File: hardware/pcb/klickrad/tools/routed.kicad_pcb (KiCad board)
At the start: 2 copper layers, 32 x 32 mm, 25 parts, among them J1 SM06B-SRSS-TB, SW1 BUTTON, SW2 WHEEL, SW3 GUARD, U1 AT42QT2120, U2 DRV2605LDGSR

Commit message: Platinen: Zwischenstand (in Arbeit)
Co-Authored-By: Claude Opus 5.5 <noreply@anthropic.com>
Claude-Session: https://claude.ai/code/session_01JifvE6gExGmwsJWDpfRrrS
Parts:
- J1: value SM06B-SRSS-TB -> FH12-6S-0.5SH; footprint Connector_JST:JST_SH_SM06B-SRSS-TB_1x06-1MP_P1.00mm_Horizontal -> Connector_FFC-FPC:Hirose_FH12-6S-0.5SH_1x06-1MP_P0.50mm_Horizontal
- moved R8 2.70 mm to (97.4, 106.3), turned to 180 degrees
- moved R7 2.06 mm to (95.2, 106.8)
- moved R9 1.20 mm to (97.4, 105.2), turned to 180 degrees
- moved J1 0.60 mm to (100.0, 110.8)
- moved C4 0.50 mm to (96.1, 102.2)
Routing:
- net EG: track 57.0 -> 11.3 mm, vias 3 -> 1
- net CHANGE: track 5.63 -> 34.9 mm, vias 2 -> 0
- net E0: track 21.6 -> 14.2 mm, vias 1 -> 3
- net SCL: track 10.5 -> 15.8 mm, vias 2 -> 3
- net 3V3: track 36.1 -> 34.8 mm
- net REG: track 2.47 -> 2.79 mm, vias 0 -> 2
- net E1: track 4.22 -> 3.91 mm, vias 3 -> 1

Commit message: Hauptplatine: platziert, nicht geroutet; Befund in KONZEPT.md
Co-Authored-By: Claude Sonnet 5.5 <noreply@anthropic.com>
Claude-Session: https://claude.ai/code/session_01JifvE6gExGmwsJWDpfRrrS
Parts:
- removed C5: 10uF, Capacitor_SMD:C_0603_1608Metric
- J1: value FH12-6S-0.5SH -> 503480-0600; footprint Connector_FFC-FPC:Hirose_FH12-6S-0.5SH_1x06-1MP_P0.50mm_Horizontal -> Klickrad:Molex_503480-0600_1x06-1MP_P0.50mm_Horizontal
- moved TP2 25.8 mm to (113.1, 104.8)
- moved TP1 25.4 mm to (113.1, 102.4)
- moved C3 17.6 mm to (110.2, 107.6), turned to 0 degrees
- moved U2 16.1 mm to (108.5, 103.6), turned to 0 degrees
- moved R7 12.7 mm to (106.4, 100.8), turned to -90 degrees
- moved C4 9.30 mm to (104.5, 106.2)
- moved C1 2.06 mm to (102.6, 105.0)
- moved C2 1.95 mm to (102.6, 103.7), turned to 90 degrees
- moved R9 1.70 mm to (98.7, 106.3), turned to 0 degrees
- moved R4 1.66 mm to (101.9, 99.0), turned to 0 degrees
- moved R3 1.32 mm to (102.9, 100.0)
- moved R5 1.02 mm to (97.4, 99.7)
- moved R1 0.90 mm to (104.8, 101.4)
- moved R2 0.90 mm to (104.8, 100.2)
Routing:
- net GND: track 0.00 -> 33.4 mm, vias 0 -> 2
- net CHANGE: track 34.9 -> 8.69 mm
- net SDA: track 12.1 -> 17.0 mm, vias 0 -> 3
- net SCL: track 15.8 -> 12.4 mm
- net LRA_N: track 4.16 -> 0.88 mm
- net 3V3: track 34.8 -> 37.9 mm, vias 2 -> 4
- net EB: track 0.45 -> 3.43 mm
- net LRA_P: track 2.82 -> 0.88 mm
- net REG: track 2.79 -> 1.25 mm, vias 2 -> 0
- net EG: track 11.3 -> 12.6 mm
- net E2: track 4.40 -> 5.62 mm
- net K0: track 1.44 -> 2.36 mm
- net K1: track 1.46 -> 2.36 mm
- net EN: track 0.45 -> 1.05 mm

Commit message: Klickrad v2 und S31-Test: Zwischenstand (in Arbeit)
Co-Authored-By: Claude Sonnet 5.5 <noreply@anthropic.com>
Claude-Session: https://claude.ai/code/session_01JifvE6gExGmwsJWDpfRrrS
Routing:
- net SCL: track 12.4 -> 21.8 mm, vias 3 -> 4
- net 3V3: track 37.9 -> 32.1 mm, vias 4 -> 0
- net GND: track 33.4 -> 31.5 mm, vias 2 -> 1
- net CHANGE: track 8.69 -> 9.75 mm
- net SDA: track 17.0 -> 16.0 mm

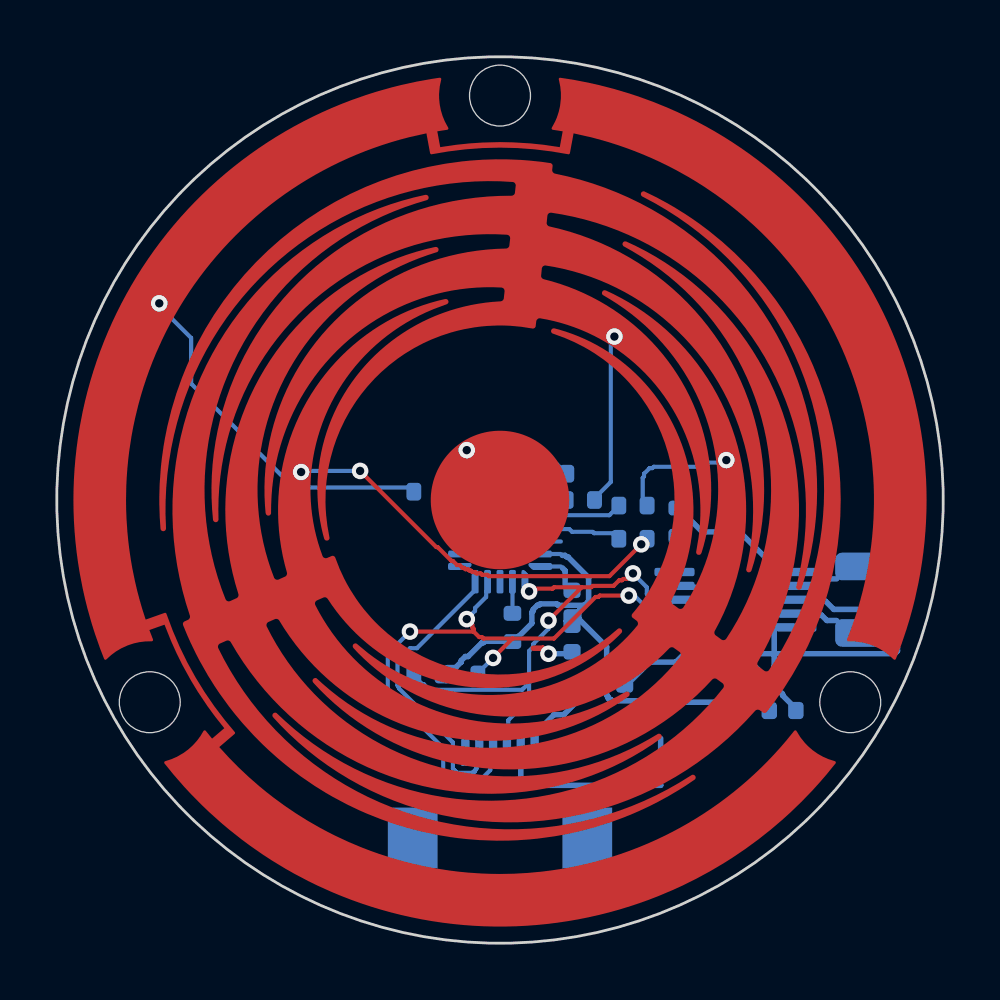
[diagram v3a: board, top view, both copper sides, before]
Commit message: S31-Buildtest-Ergebnis und offene Punkte dokumentiert
Co-Authored-By: Claude Sonnet 5.5 <noreply@anthropic.com>
Claude-Session: https://claude.ai/code/session_01JifvE6gExGmwsJWDpfRrrS
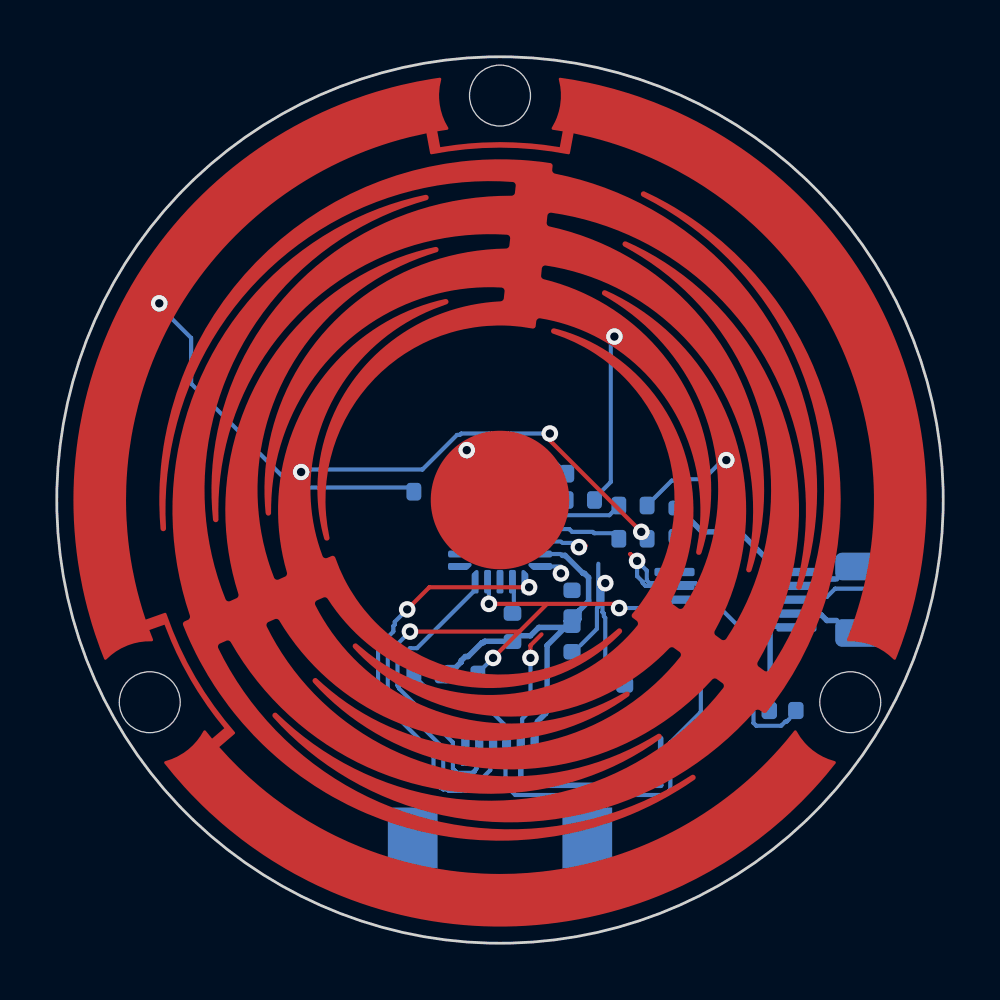
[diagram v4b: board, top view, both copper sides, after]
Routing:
- net SDA: track 16.0 -> 34.8 mm, vias 3 -> 2
- net 3V3: track 32.1 -> 23.2 mm
- net GND: track 31.5 -> 38.0 mm, vias 1 -> 5
- net E1: track 3.84 -> 3.01 mm
- net SCL: track 21.8 -> 22.4 mm

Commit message: Klickrad v2 fertig: TEILE.md und Problemliste aktualisiert
Co-Authored-By: Claude Sonnet 5.5 <noreply@anthropic.com>
Claude-Session: https://claude.ai/code/session_01JifvE6gExGmwsJWDpfRrrS
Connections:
- U1 pad 21: (no net) -> GND
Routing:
- net 3V3: track 23.2 -> 43.7 mm, vias 0 -> 2
- net SDA: track 34.8 -> 14.6 mm, vias 2 -> 3
- net GND: track 38.0 -> 32.2 mm, vias 5 -> 3
- net LRA_N: track 0.88 -> 2.72 mm
- net LRA_P: track 0.88 -> 2.72 mm
- net SCL: track 22.4 -> 21.8 mm

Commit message: Klickrad J1 auf J21-Landmuster, neu geroutet; TEILE-Nachtrag
Co-Authored-By: Claude Sonnet 5.5 <noreply@anthropic.com>
Claude-Session: https://claude.ai/code/session_01JifvE6gExGmwsJWDpfRrrS
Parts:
- J1: footprint Klickrad:Molex_503480-0600_1x06-1MP_P0.50mm_Horizontal -> Klickrad:Molex_503480-0600_Hauptplatine
- turned J1 to 0 degrees
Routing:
- net 3V3: track 43.7 -> 57.3 mm, vias 2 -> 4
- net SDA: track 14.6 -> 18.2 mm, vias 3 -> 2
- net SCL: track 21.8 -> 25.1 mm
- net E0: track 14.1 -> 16.1 mm
- net CHANGE: track 9.75 -> 11.7 mm
- net EG: track 12.6 -> 11.5 mm
- net LRA_P: track 2.72 -> 3.64 mm
- net GND: track 32.2 -> 31.6 mm
